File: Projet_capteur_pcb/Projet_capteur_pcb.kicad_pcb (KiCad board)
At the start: 2 copper layers, 68.6 x 53.3 mm, 22 parts, among them J1 Power, J2 Digital/PWM, J3 Analog, J4 Digital/PWM

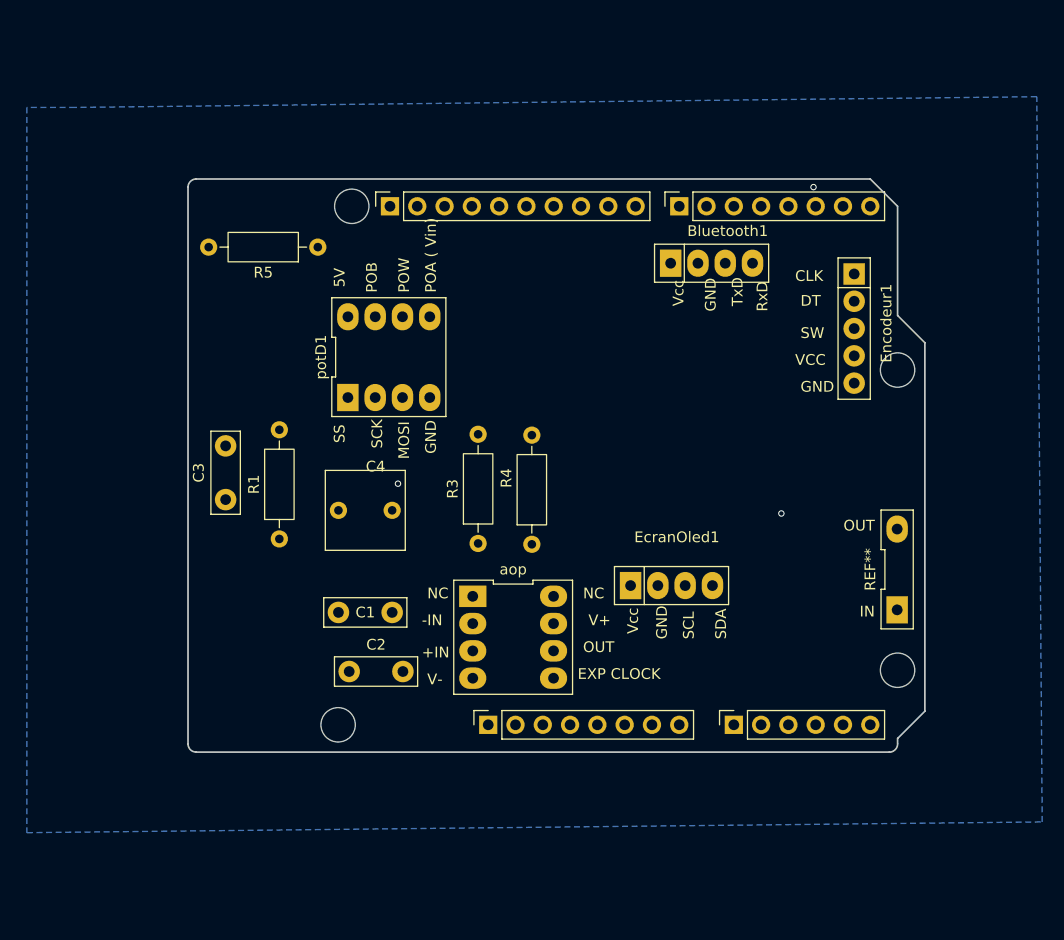
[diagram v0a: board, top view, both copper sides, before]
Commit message: changement pin
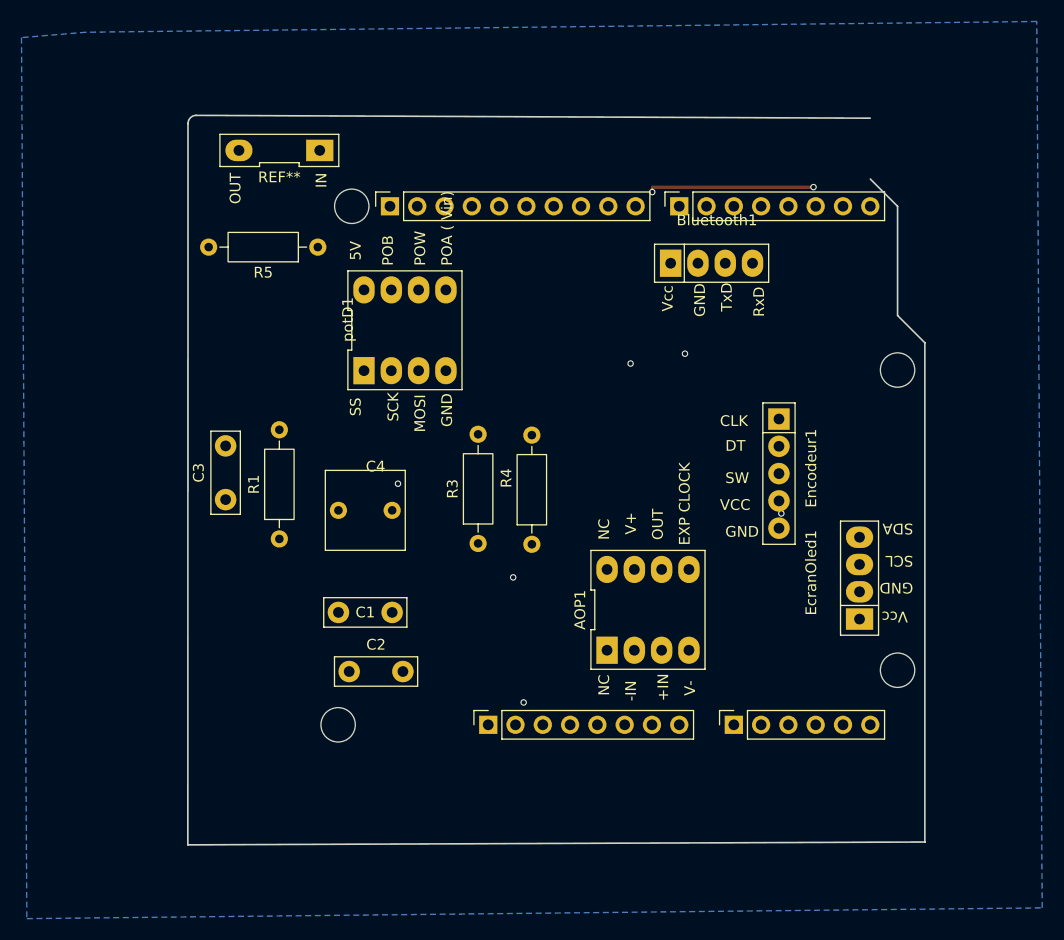
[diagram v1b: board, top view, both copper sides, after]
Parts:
- removed aop: AOP, Librairie_empreinte:DIP-8_296_ELL
- added AOP1: ~, Librairie_empreinte:AO, F.Cu at (142.8, 86.8)
- Bluetooth1: footprint Librairie_empreinte:SIP-4 -> Librairie_empreinte:Empreinte_bluetooth
- moved REF** 69.5 mm to (108.5, 44.0), turned to 90 degrees
- moved EcranOled1 17.5 mm to (162.5, 83.8), turned to 90 degrees
- moved Encodeur1 15.2 mm to (155.0, 74.1)
- moved potD1 2.92 mm to (120.2, 60.7)
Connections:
- J1 pad 8: +5V -> VCC
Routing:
- net SCL: track 0.00 -> 15.5 mm, vias 1 -> 2
- net adc: vias 0 -> 1
- net SDA: vias 0 -> 1
- net Net-(AOP1-OUT): vias 1 -> 0
- net +5V: vias 0 -> 3
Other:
- board size 68.6 x 53.3 mm -> 68.6 x 67.9 mm

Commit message: pcb
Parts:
- moved potD1 10.5 mm to (130.5, 59.0)
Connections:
- potD1 pad 1: (no net) -> CS
- potD1 pad 2: (no net) -> SCK
- potD1 pad 3: (no net) -> MOSI
- potD1 pad 4: (no net) -> GND
- potD1 pad 5: (no net) -> +5V
- potD1 pad 6: (no net) -> GND
- potD1 pad 7: (no net) -> GND
- potD1 pad 8: (no net) -> GND
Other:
- outline, holes or cut-outs redrawn
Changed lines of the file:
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@@
 	(footprint "Librairie_empreinte:dig pot"
 		(layer "F.Cu")
-		(at 120.19 60.74)
+		(at 130.5 59)
 		(property "Reference" "potD1"
 			(at -5.31 -1 90)
@@
 			)
 		)
-		(fp_text user "SS"
+		(fp_text user "CS"
 			(at -4 8 90)
 			(unlocked yes)
@@
 			(layers "*.Cu" "*.Mask")
 			(remove_unused_layers no)
+			(net 31 "CS")
+			(pinfunction "CS")
+			(pintype "input")
 			(thermal_bridge_angle 45)
 		)
@@
 			(layers "*.Cu" "*.Mask")
 			(remove_unused_layers no)
+			(net 30 "SCK")
+			(pinfunction "SCK")
+			(pintype "input")
 			(thermal_bridge_angle 45)
 		)
@@
 			(layers "*.Cu" "*.Mask")
 			(remove_unused_layers no)
+			(net 29 "MOSI")
+			(pinfunction "SI")
+			(pintype "input")
 			(thermal_bridge_angle 45)
 		)
@@
 			(layers "*.Cu" "*.Mask")
 			(remove_unused_layers no)
+			(net 1 "GND")
+			(pinfunction "Vss")
+			(pintype "input")
 			(thermal_bridge_angle 45)
 		)
@@
 			(layers "*.Cu" "*.Mask")
 			(remove_unused_layers no)
+			(net 3 "+5V")
+			(pinfunction "VDD")
+			(pintype "input")
 			(thermal_bridge_angle 45)
 		)
@@
 			(layers "*.Cu" "*.Mask")
 			(remove_unused_layers no)
+			(net 1 "GND")
+			(pinfunction "PBO")
+			(pintype "input")
 			(thermal_bridge_angle 45)
 		)
@@
 			(layers "*.Cu" "*.Mask")
 			(remove_unused_layers no)
+			(net 1 "GND")
+			(pinfunction "PW0")
+			(pintype "input")
 			(thermal_bridge_angle 45)
 		)
@@
 			(layers "*.Cu" "*.Mask")
 			(remove_unused_layers no)
+			(net 1 "GND")
+			(pinfunction "PA0")
+			(pintype "input")
 			(thermal_bridge_angle 45)
 		)
@@
 	)
 	(gr_line
-		(start 163.5 46.66)
-		(end 166.04 49.2)
+		(start 163.23 40.73)
+		(end 166.04 43.54)
 		(stroke
 			(width 0.15)
@@
 	)
 	(gr_line
-		(start 166.04 49.2)
+		(start 166.04 43.54)
 		(end 166.04 59.36)
 		(stroke

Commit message: routage
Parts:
- moved REF** 60.5 mm to (107.8, 104.5)
- moved R5 40.8 mm to (124.1, 92.0)
- moved AOP1 34.6 mm to (116.8, 64.0), turned to 180 degrees
- moved C2 30.6 mm to (145.5, 90.5), turned to 90 degrees
- moved C3 28.6 mm to (119.0, 100.5), turned to -90 degrees
- moved R4 23.9 mm to (153.0, 92.1)
- moved Bluetooth1 23.1 mm to (143.3, 77.0)
- moved C4 20.6 mm to (132.0, 87.5)
- moved Encodeur1 15.2 mm to (161.0, 60.1)
- moved potD1 7.86 mm to (138.3, 60.3), turned to -90 degrees
- moved R3 5.10 mm to (132.0, 79.6)
- moved C1 5.00 mm to (119.0, 87.0)
- moved R1 3.96 mm to (106.5, 83.6)
- moved EcranOled1 1.80 mm to (164.0, 82.8), turned to -90 degrees
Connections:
- AOP1 pad 2: GND -> Net-(AOP1--IN)
- C4 pad 1: GND -> Net-(AOP1--IN)
- R3 pad 2: GND -> Net-(AOP1--IN)
- potD1 pad 8: GND -> Net-(AOP1--IN)
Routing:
- net Net-(AOP1-+IN): track 0.00 -> 68.5 mm, vias 1 -> 0
- net SCL: track 15.5 -> 78.9 mm, vias 2 -> 3
- net +5V: track 0.00 -> 27.5 mm
- net Rxd: track 0.00 -> 21.8 mm, vias 0 -> 1
- net Net-(C6-OUT): track 0.00 -> 10.6 mm
- net TxD: track 0.00 -> 10.4 mm, vias 0 -> 1
- net CLK: track 0.00 -> 3.22 mm
- net MOSI: track 0.00 -> 1.67 mm
- net DT: track 0.00 -> 0.68 mm
- net Net-(AOP1-OUT): vias 0 -> 1
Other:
- outline, holes or cut-outs redrawn
- board text added: "-IN"

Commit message: routage V1
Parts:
- removed C3: C, Capacitor_THT:C_Disc_D7.5mm_W2.5mm_P5.00mm
- removed REF**: CAPTEUR, Librairie_empreinte:CAPTEUR
- added capteur1: ~, Librairie_empreinte:DIP-2_296_ELL, F.Cu at (132.0, 102.5)
- C1, C2: value C -> 100n
- C4: value C -> 1u
- R1, R3: value R -> 100k
- R4: value R -> 1k
- R5: value R -> 10K
- moved EcranOled1 64.0 mm to (110.0, 48.5), turned to 90 degrees
- moved C2 13.5 mm to (158.5, 87.0), turned to -90 degrees
- moved R4 12.5 mm to (140.5, 93.1)
- moved R5 11.0 mm to (124.1, 103.0)
- moved C4 5.59 mm to (126.5, 88.5)
- moved C1 3.81 mm to (115.5, 85.5)
- moved Encodeur1 3.04 mm to (158.0, 59.6)
- moved Bluetooth1 2.54 mm to (140.8, 77.0)
- moved potD1 2.28 mm to (136.0, 60.0), turned to 180 degrees
- moved AOP1 2.02 mm to (116.5, 62.0), turned to 0 degrees
- moved R3 0.50 mm to (131.5, 79.6)
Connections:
- net /A1 renamed flex_out
- net Net-(AOP1--IN) renamed potor_out
- net adc renamed ampli_out
- AOP1 pad 4: (no net) -> GND
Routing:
- net GND: track 0.00 -> 243.3 mm
- net +5V: track 27.5 -> 156.9 mm, vias 3 -> 0
- net MOSI: track 1.67 -> 72.6 mm
- net SCL: track 78.9 -> 9.61 mm, vias 3 -> 0
- net Net-(AOP1-OUT): track 0.00 -> 51.1 mm, vias 1 -> 0
- net potor_out: track 0.11 -> 40.1 mm
- net TxD: track 10.4 -> 46.4 mm, vias 1 -> 0
- net ampli_out: track 0.00 -> 33.3 mm, vias 1 -> 0
- net Rxd: track 21.8 -> 43.2 mm, vias 1 -> 0
- net Net-(AOP1-+IN): track 68.5 -> 53.4 mm
- net SW: track 0.27 -> 13.9 mm
- net SDA: track 0.00 -> 13.6 mm, vias 1 -> 0
- net SCK: track 0.00 -> 11.4 mm
- net CS: track 0.00 -> 9.69 mm
- net DT: track 0.68 -> 10.3 mm
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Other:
- board text added: "GND"
- board text removed: "-IN"
